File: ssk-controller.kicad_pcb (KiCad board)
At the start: 2 copper layers, 170 x 50 mm, 33 parts, among them J1 Conn_01x16, J2 Conn_01x08, J3 Conn_01x01, J4 USB_B, J5 Solenoid, Q1 Q_NMOS_GDS, SW1 SW_Push, U1 ATmega32U4-AU, U2 PRTR5V0U2X, Y1 16Mhz

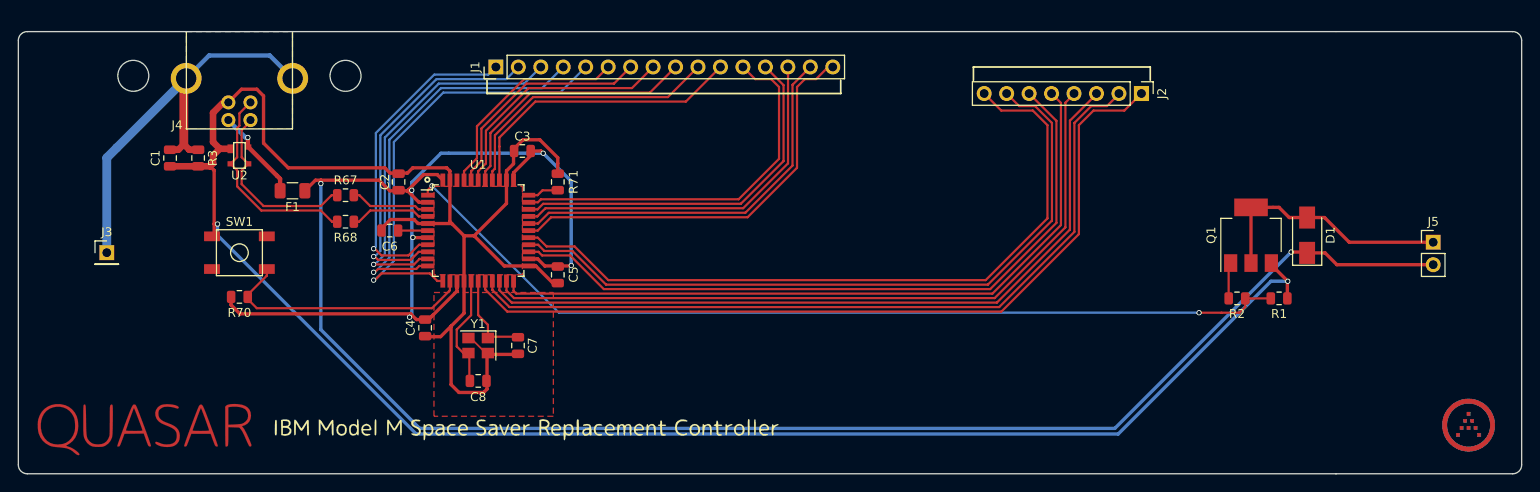
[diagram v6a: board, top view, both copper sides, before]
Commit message: Update to 2.0 gerbers
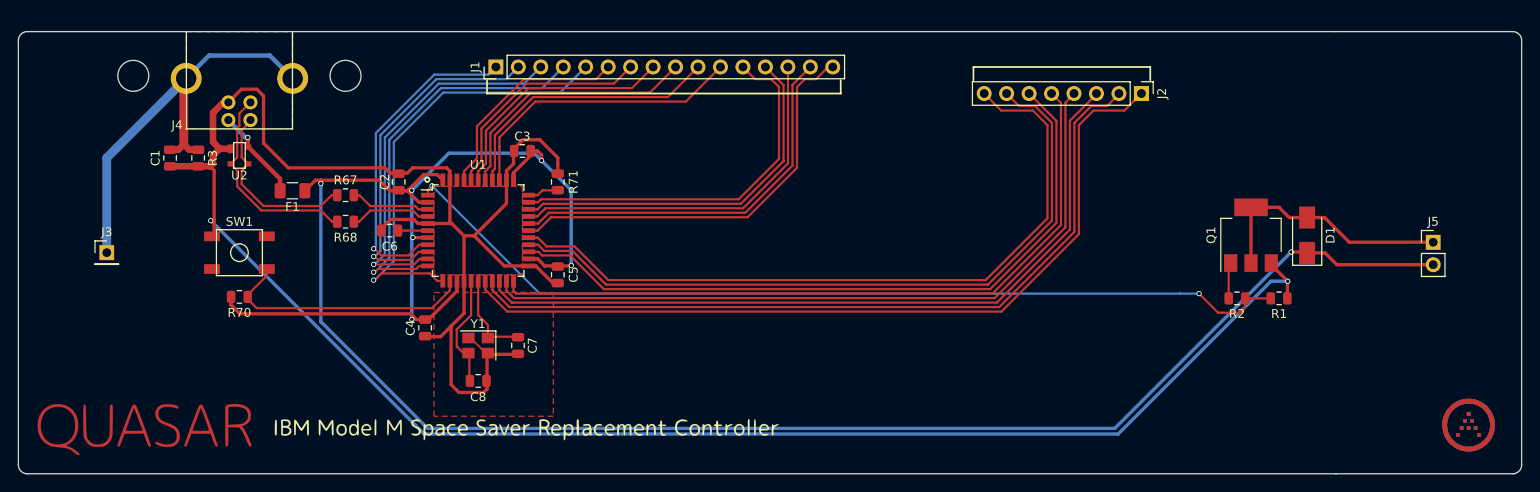
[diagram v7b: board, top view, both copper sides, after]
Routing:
- net +5V: track 266.4 -> 265.5 mm
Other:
- board text added: "Rev 2.0 20200323"
- board text removed: "Rev 1.2 20190527"
- board text removed: "When installing sockets, compare the orientation to the stock controller"

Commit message: Add both 9V and 5V solenoid compat
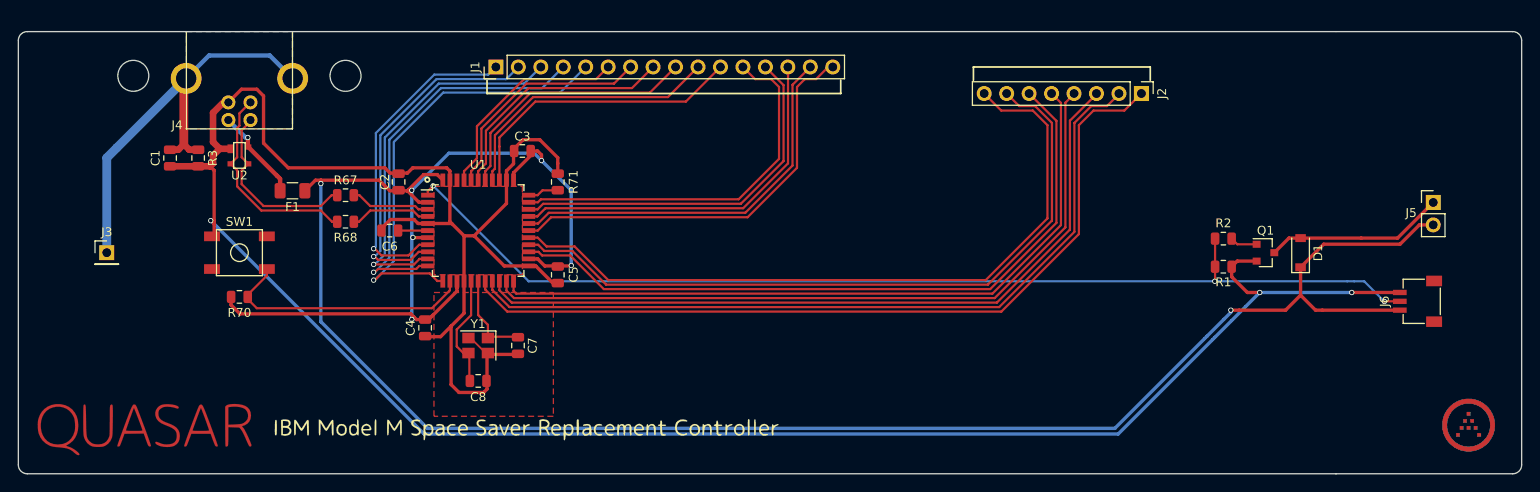
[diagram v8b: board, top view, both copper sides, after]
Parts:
- added J6: Solenoid_Signal, random-keyboard-parts:JST-SR-3, F.Cu at (251.0, 80.5)
- D1: footprint Diode_SMD:D_SMA -> Diode_SMD:D_SOD-123
- Q1: value Q_NMOS_GDS -> Q_NMOS_GSD; footprint Package_TO_SOT_SMD:SOT-223-3_TabPin2 -> Package_TO_SOT_SMD:SOT-23
- moved R1 7.25 mm to (226.3, 76.6)
- moved R2 6.93 mm to (226.3, 73.4), turned to 180 degrees
- moved J5 4.50 mm to (250.0, 69.3)
- moved Q1 2.57 mm to (231.0, 75.0), turned to 0 degrees
- moved D1 2.11 mm to (235.0, 75.0)
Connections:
- Q1 pad 2: Net-(D1-Pad2) -> GND
- Q1 pad 3: GND -> Net-(D1-Pad2)
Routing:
- net SOLENOID: track 103.3 -> 120.9 mm, vias 2 -> 3
- net GND: track 285.5 -> 301.0 mm, vias 2 -> 3
- net +5V: track 265.5 -> 280.1 mm
- net Net-(D1-Pad2): track 28.5 -> 20.3 mm
- net Net-(Q1-Pad1): track 4.09 -> 3.09 mm
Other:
- board text added: "5V Solenoid Direct"
- board text added: "JST SR 3-Pin for Unified Daughterboard S9"
- board text added: "Rev 2.1 20200331"
- board text removed: "5V solenoid"
- board text removed: "Rev 2.0 20200323"
